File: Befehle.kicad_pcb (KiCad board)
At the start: 2 copper layers, 60 parts, among them J1 2PinTerminalBlocktg, J2 2PinTerminalBlocktg, J3 3PinTerminalBlocktg, J4 2PinTerminalBlocktg, J5 2PinTerminalBlocktg, P1 CONN_02X10, P2 CONN_02X10, U1 74LS14, U2 74540, U3 7400, U4 74HCT02, U5 74LS541, U6 74LS373, U7 74LS139, U8 74LS540

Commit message: overview and speicher
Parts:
- added REF**: EuroBoard160mmX100mm_holes, tg_locallibs:EuroBoard160mmX100mm_holes, F.Cu at (116.9, 180.1)
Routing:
- net Net-(R7-Pad1): track 137.4 -> 143.8 mm
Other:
- board outline added: 100 x 160 mm

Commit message: Akku pc finished
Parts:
- moved D22 3.41 mm to (43.9, 27.5)
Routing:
- net GND: track 702.7 -> 704.0 mm
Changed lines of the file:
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@@
     (thickness 1.6)
     (drawings 2)
-    (tracks 839)
+    (tracks 840)
     (zones 0)
     (modules 61)
@@
   )
   (module Diodes_ThroughHole:D_DO-41_SOD81_P10.16mm_Horizontal (layer F.Cu)
-    (at 40.5 27.5)
+    (at 43.91 27.5)
     (descr "D, DO-41_SOD81 series, Axial, Horizontal, pin pitch=10.16mm, , length*diameter=5.2*2.7mm^2, , http://www.diodes.com/_files/packages/DO-41%20(Plastic).pdf")
     (tags "D DO-41_SOD81 series Axial Horizontal pin pitch 10.16mm  length 5.2mm diameter 2.7mm")
@@
   (segment (start 31.5 89.5) (end 33.74 89.5) (width 1.25) (layer B.Cu) (net 14) (status 20))
   (segment (start 33.74 89.5) (end 34 89.24) (width 1.25) (layer B.Cu) (net 14) (status 30))
-  (segment (start 71.5 67) (end 71.5 55.5) (width 1.25) (layer B.Cu) (net 14))
-  (segment (start 70.5 27.5) (end 50.66 27.5) (width 1.25) (layer B.Cu) (net 14) (status 20))
-  (segment (start 70.5 54.5) (end 70.5 27.5) (width 1.25) (layer B.Cu) (net 14))
-  (segment (start 71.5 55.5) (end 70.5 54.5) (width 1.25) (layer B.Cu) (net 14))
   (segment (start 81 67) (end 76 67) (width 1.25) (layer B.Cu) (net 14) (status 10))
   (segment (start 76 67) (end 71.5 67) (width 1.25) (layer B.Cu) (net 14))
@@
   (segment (start 98.5 99) (end 81 99) (width 1.25) (layer B.Cu) (net 14))
   (segment (start 98.78 99.28) (end 98.5 99) (width 1.25) (layer B.Cu) (net 14))
-  (segment (start 32.5 27.5) (end 22 27.5) (width 2) (layer B.Cu) (net 14) (status 10))
-  (segment (start 19.5 30) (end 19.5 32) (width 2) (layer B.Cu) (net 14))
-  (segment (start 19.5 32) (end 19.5 34.4) (width 2) (layer B.Cu) (net 14))
   (segment (start 19.5 34.4) (end 19.5 34.5) (width 2) (layer B.Cu) (net 14))
   (segment (start 19.5 34.5) (end 19.5 37.3) (width 2) (layer B.Cu) (net 14))
@@
   (segment (start 19.5 89.5) (end 19.5 132.25) (width 2) (layer B.Cu) (net 14))
   (segment (start 19.5 132.25) (end 19.5 156.25) (width 2) (layer B.Cu) (net 14))
+  (segment (start 70.5 27.5) (end 54.07 27.5) (width 1.25) (layer B.Cu) (net 14))
+  (segment (start 70.5 54.5) (end 70.5 27.5) (width 1.25) (layer B.Cu) (net 14))
+  (segment (start 71.5 67) (end 71.5 55.5) (width 1.25) (layer B.Cu) (net 14))
+  (segment (start 71.5 55.5) (end 70.5 54.5) (width 1.25) (layer B.Cu) (net 14))
+  (segment (start 19.5 32) (end 19.5 34.4) (width 2) (layer B.Cu) (net 14))
+  (segment (start 19.5 30) (end 19.5 32) (width 2) (layer B.Cu) (net 14))
   (segment (start 22 27.5) (end 19.5 30) (width 2) (layer B.Cu) (net 14))
-  (segment (start 50.66 27.5) (end 50.5 27.5) (width 2) (layer B.Cu) (net 14) (status 30))
-  (segment (start 50.5 27.5) (end 46 32) (width 2) (layer B.Cu) (net 14) (status 10))
-  (segment (start 46 32) (end 34 32) (width 2) (layer B.Cu) (net 14))
+  (segment (start 54.07 29.56) (end 51.63 32) (width 2) (layer B.Cu) (net 14))
+  (segment (start 54.07 27.5) (end 54.07 29.56) (width 2) (layer B.Cu) (net 14))
+  (segment (start 32.5 27.5) (end 22 27.5) (width 2) (layer B.Cu) (net 14))
+  (segment (start 51.63 32) (end 34 32) (width 2) (layer B.Cu) (net 14))
   (segment (start 34 32) (end 32.5 30.5) (width 2) (layer B.Cu) (net 14))
-  (segment (start 32.5 30.5) (end 32.5 27.5) (width 2) (layer B.Cu) (net 14) (status 20))
+  (segment (start 32.5 30.5) (end 32.5 27.5) (width 2) (layer B.Cu) (net 14))
   (segment (start 105 36.46) (end 100 36.46) (width 1) (layer B.Cu) (net 15) (status C00000))
   (segment (start 110 36.46) (end 105 36.46) (width 1) (layer B.Cu) (net 15) (status C00000))
@@
   (segment (start 113.62 146.5) (end 113.5 146.5) (width 1.25) (layer B.Cu) (net 15))
   (segment (start 114 146.12) (end 113.62 146.5) (width 1.25) (layer B.Cu) (net 15))
-  (segment (start 44.5 22) (end 39 27.5) (width 2) (layer B.Cu) (net 15))
-  (segment (start 114 30.5) (end 114 36.5) (width 2) (layer B.Cu) (net 15))
   (segment (start 114 36.5) (end 114 97) (width 2) (layer B.Cu) (net 15))
   (segment (start 114 97) (end 114 112) (width 2) (layer B.Cu) (net 15))
   (segment (start 114 112) (end 114 146.5) (width 2) (layer B.Cu) (net 15))
   (segment (start 114 146.5) (end 114 167.5) (width 2) (layer B.Cu) (net 15))
-  (segment (start 105.5 22) (end 114 30.5) (width 2) (layer B.Cu) (net 15))
-  (segment (start 44.5 22) (end 105.5 22) (width 2) (layer B.Cu) (net 15))
   (segment (start 37 27.5) (end 39 27.5) (width 2) (layer B.Cu) (net 15) (status 10))
   (segment (start 39 27.5) (end 40.5 27.5) (width 2) (layer B.Cu) (net 15) (status 20))
@@
   (segment (start 84.5 175.55) (end 84.5 177) (width 1.25) (layer B.Cu) (net 15))
   (segment (start 84.5 174.5) (end 84.5 175.55) (width 1.25) (layer B.Cu) (net 15))
+  (segment (start 43.91 27.5) (end 39 27.5) (width 2) (layer B.Cu) (net 15))
+  (segment (start 49.41 22) (end 43.91 27.5) (width 2) (layer B.Cu) (net 15))
+  (segment (start 114 36.5) (end 114 30.5) (width 2) (layer B.Cu) (net 15))
+  (segment (start 105.5 22) (end 49.41 22) (width 2) (layer B.Cu) (net 15))
+  (segment (start 114 30.5) (end 105.5 22) (width 2) (layer B.Cu) (net 15))
   (segment (start 39.25 150.08) (end 39.25 147.5) (width 0.2) (layer B.Cu) (net 16))
   (segment (start 39.29 147.54) (end 41.62 147.54) (width 0.2) (layer B.Cu) (net 16) (status 20))

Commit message: BIB Cleanup finished
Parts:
- D11, D12, D15, D16, D19, D20: footprint tg_foodprint:Diode_D1.8mm_W3.3mm_H2.4mmBonsai -> allBonsaiFootprintsLibs:Diode_D1.8mm_W3.3mm_H2.4mmBonsai
- P1, P2: footprint tg_foodprint:Pin_Header_Straight_2x10_Pitch2.00mmBonsai.pretty -> allBonsaiFootprintsLibs:Pin_Header_Straight_2x10_Pitch2.00mmBonsai.pretty
- U1, U3, U4: footprint tg_foodprint:DIP-14_W7.62mm_Socket_LongPadstg -> allBonsaiFootprintsLibs:DIP-14_W7.62mm_Socket_LongPadstg
- U2: footprint Housings_DIP:DIP-20_W7.62mm_Socket_LongPads -> allBonsaiFootprintsLibs:DIP-20_W7.62mm_Socket_LongPadstg
- U5, U6, U8: footprint tg_foodprint:DIP-20_W7.62mm_Socket_LongPadstg -> allBonsaiFootprintsLibs:DIP-20_W7.62mm_Socket_LongPadstg
- U7: footprint tg_foodprint:DIP-16_W7.62mm_Socket_LongPadstg -> allBonsaiFootprintsLibs:DIP-16_W7.62mm_Socket_LongPadstg
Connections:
- U1 pad 8: Net-(U1-Pad8) -> (no net)

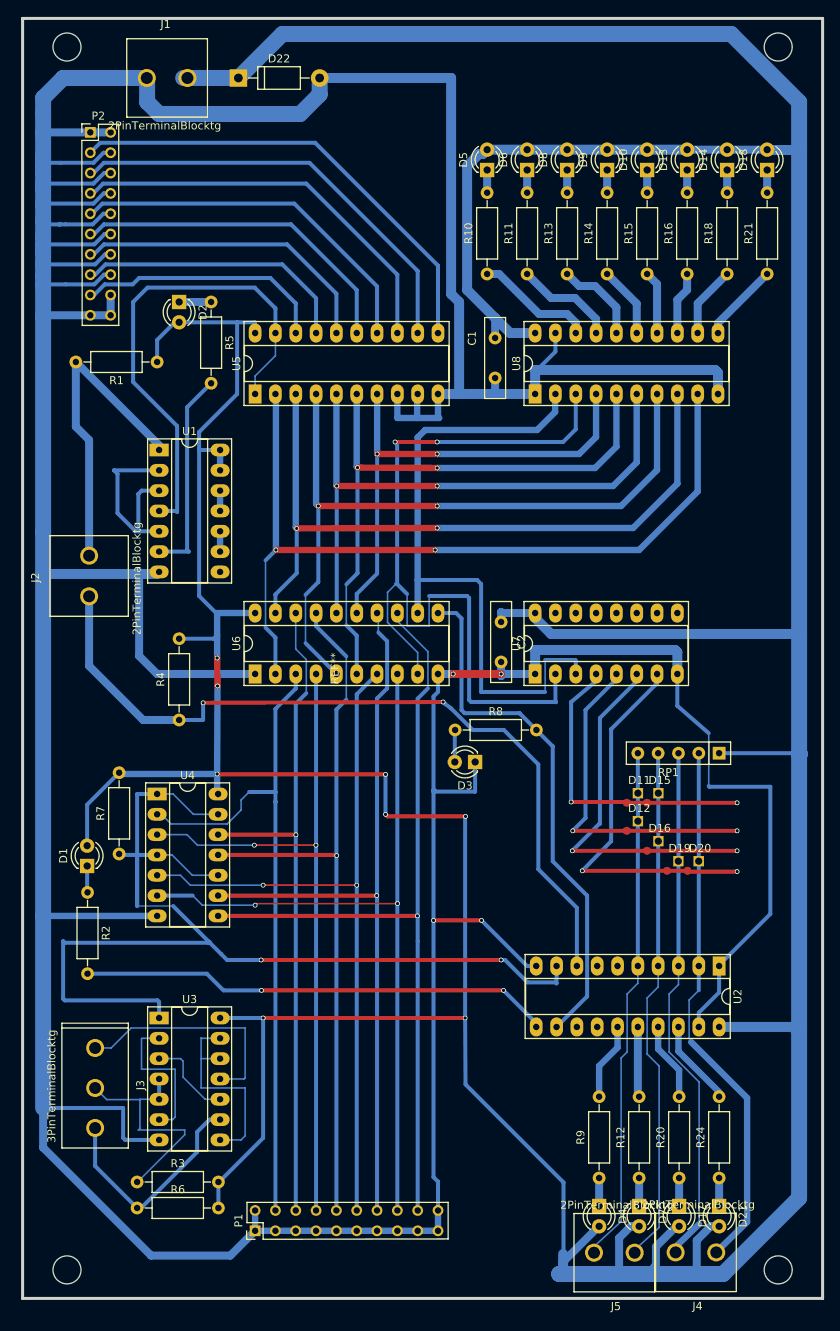
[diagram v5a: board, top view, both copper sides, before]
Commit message: Footprint Labes set invisible
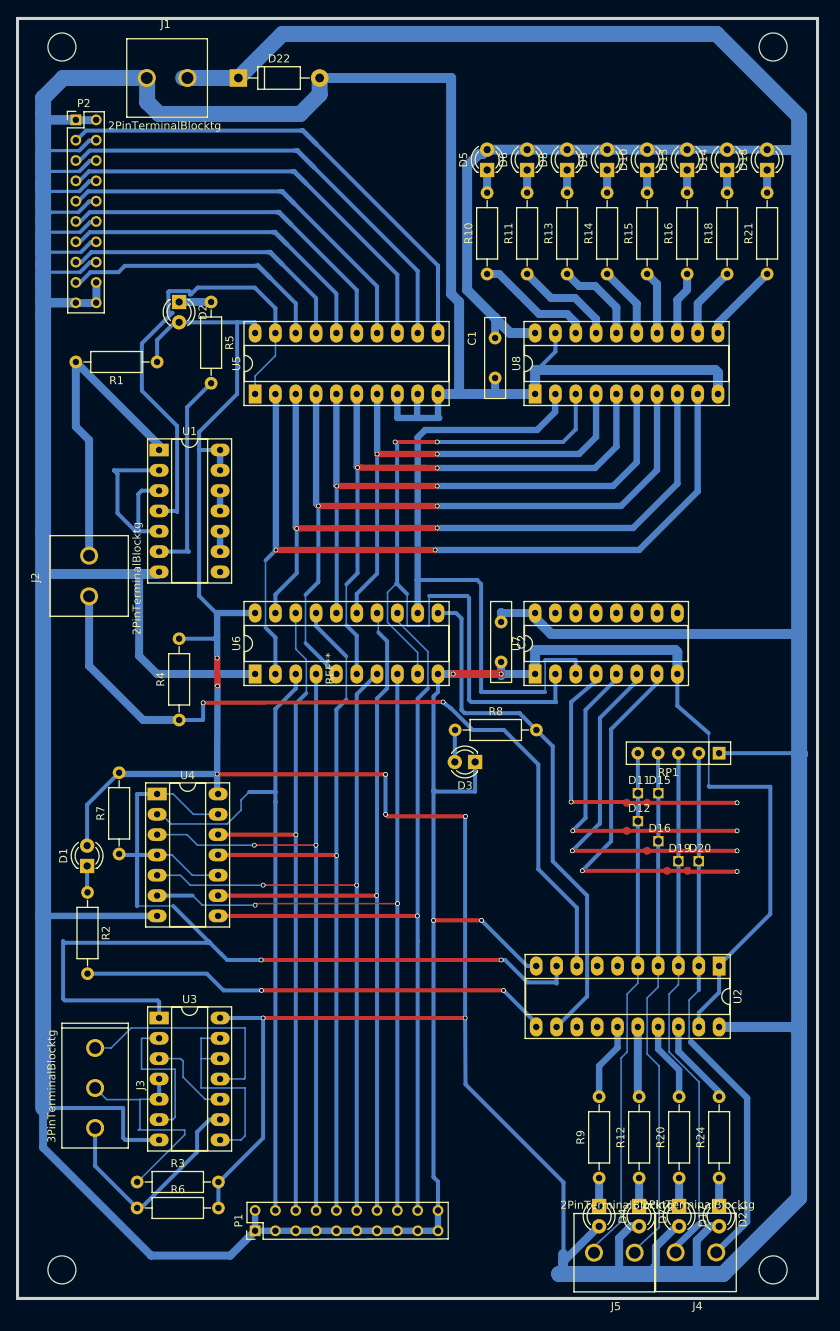
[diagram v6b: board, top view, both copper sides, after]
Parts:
- moved P2 2.39 mm to (23.6, 32.7)
- moved REF** 0.64 mm to (116.3, 180.1)
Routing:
- net GND: track 704.0 -> 690.1 mm
- net Net-(P2-Pad3): track 54.8 -> 58.0 mm
- net Net-(P2-Pad2): track 58.8 -> 61.4 mm
- net Net-(P2-Pad9): track 31.6 -> 34.0 mm
- net Net-(P2-Pad5): track 46.5 -> 48.9 mm
- net Net-(P2-Pad4): track 50.9 -> 53.3 mm
- net Net-(P2-Pad7): track 38.7 -> 41.2 mm
- net Net-(P2-Pad6): track 42.6 -> 45.1 mm
- net Net-(P2-Pad8): track 34.9 -> 37.3 mm
- net Net-(U1-Pad4): track 62.2 -> 60.7 mm
- net VCC: track 696.2 -> 695.2 mm

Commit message: labeling
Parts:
- moved D21 3.69 mm to (104.2, 164.8)
- moved D4 3.69 mm to (89.0, 164.8)
- moved D17 3.69 mm to (99.0, 164.8)
- moved D7 3.69 mm to (94.0, 164.8)
- moved R24 3.37 mm to (104.2, 161.6)
- moved R9 3.36 mm to (89.0, 161.6)
- moved R12 3.36 mm to (94.0, 161.6)
- moved R20 3.36 mm to (99.0, 161.6)
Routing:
- net VCC: track 695.2 -> 710.2 mm
- net Net-(R20-Pad2): track 9.81 -> 6.45 mm
- net Net-(R12-Pad2): track 8.79 -> 5.43 mm
- net Net-(R9-Pad2): track 9.67 -> 6.87 mm
- net 0: track 67.6 -> 70.4 mm
- net Net-(R24-Pad2): track 11.1 -> 8.98 mm
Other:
- board text added: "+"
- board text added: "-"
- board text added: "Befehle"
- board text added: "write"
- board text added: "~enIR"
- board text added: "~incPC"
- board text added: "~inczPC"
- board text added: "~loadIR"
- board text added: "~upPC"

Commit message: branding
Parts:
- added G***: LOGO, allBonsaiFootprintsLibs:agi5, F.Cu at (56.0, 45.4)
